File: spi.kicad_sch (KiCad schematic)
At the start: 3 parts, among them J3 Micro_SD_Card

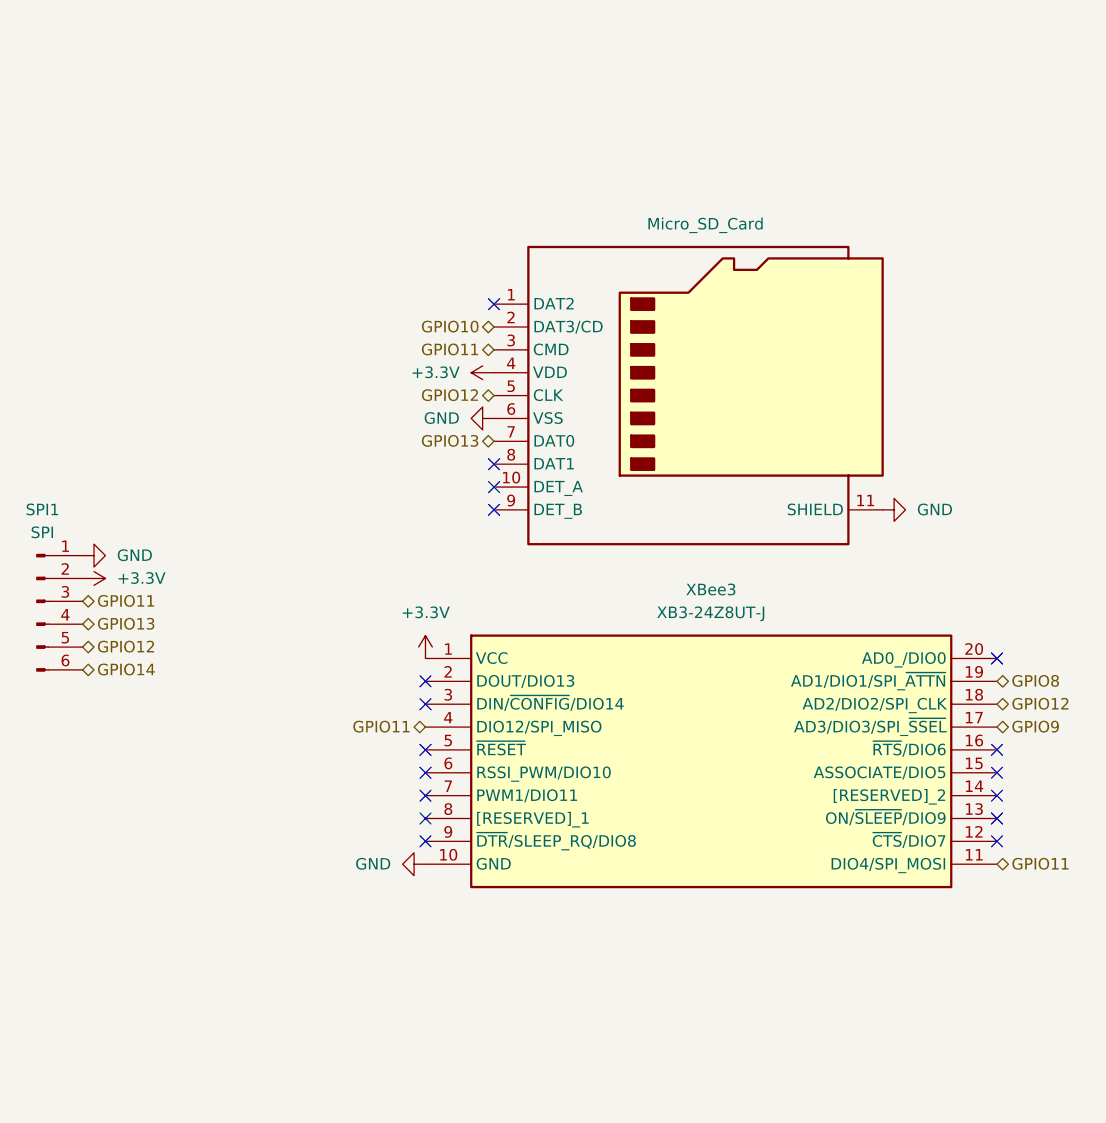
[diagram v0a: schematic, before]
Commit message: Remapped GPIOs for clean routing
This updates the GPIO table so that the traces and vias are far cleaner. Slight repositioning of some pins to account for that. Rebuilt all gerbers and necessary stuff.
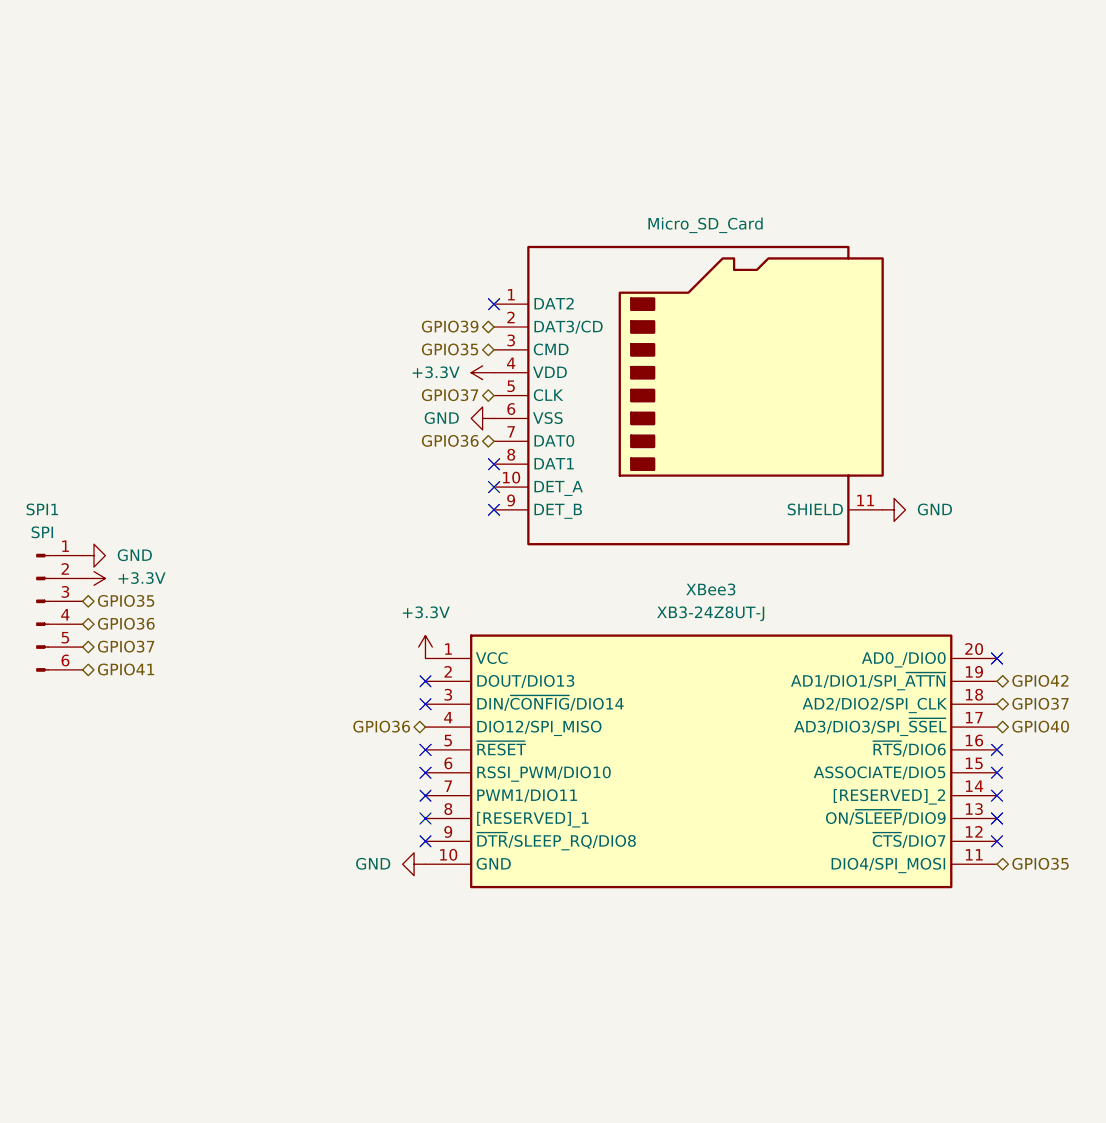
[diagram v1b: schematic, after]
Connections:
- net GPIO10 renamed GPIO39
- net GPIO11 renamed GPIO35
- net GPIO35: no longer XBee3.4 (DIO12/SPI_MISO)
- net GPIO12 renamed GPIO37
- net GPIO13 renamed GPIO36
- net GPIO36: now also XBee3.4 (DIO12/SPI_MISO)
- net GPIO14 renamed GPIO41
- net GPIO8 renamed GPIO42
- net GPIO9 renamed GPIO40
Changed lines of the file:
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@@
 		(at 110.49 100.33)
 	)
-	(hierarchical_label "GPIO11"
+	(hierarchical_label "GPIO35"
 		(shape bidirectional)
 		(at 118.11 63.5 180)
@@
 			(justify right)
 		)
-		(property "GPIO11" ""
+		(property "GPIO35" ""
 			(at 118.11 64.77 0)
 			(effects
@@
 		)
 	)
-	(hierarchical_label "GPIO14"
+	(hierarchical_label "GPIO41"
 		(shape bidirectional)
 		(at 72.39 99.06 0)
@@
 			(justify left)
 		)
-		(property "GPIO14" ""
+		(property "GPIO41" ""
 			(at 72.39 100.33 0)
 			(effects
@@
 		)
 	)
-	(hierarchical_label "GPIO11"
+	(hierarchical_label "GPIO35"
 		(shape bidirectional)
 		(at 72.39 91.44 0)
@@
 			(justify left)
 		)
-		(property "GPIO11" ""
+		(property "GPIO35" ""
 			(at 72.39 92.71 0)
 			(effects
@@
 		)
 	)
-	(hierarchical_label "GPIO11"
+	(hierarchical_label "GPIO40"
+		(shape bidirectional)
+		(at 173.99 105.41 0)
+		(fields_autoplaced yes)
+		(effects
+			(font
+				(size 1.27 1.27)
+			)
+			(justify left)
+		)
+		(property "GPIO40" ""
+			(at 173.99 106.68 0)
+			(effects
+				(font
+					(size 1.27 1.27)
+					(italic yes)
+				)
+				(justify left)
+			)
+		)
+	)
+	(hierarchical_label "GPIO36"
+		(shape bidirectional)
+		(at 110.49 105.41 180)
+		(fields_autoplaced yes)
+		(effects
+			(font
+				(size 1.27 1.27)
+			)
+			(justify right)
+		)
+		(property "GPIO36" ""
+			(at 110.49 106.68 0)
+			(effects
+				(font
+					(size 1.27 1.27)
+					(italic yes)
+				)
+				(justify right)
+			)
+		)
+	)
+	(hierarchical_label "GPIO35"
 		(shape bidirectional)
 		(at 173.99 120.65 0)
@@
 			(justify left)
 		)
-		(property "GPIO11" ""
+		(property "GPIO35" ""
 			(at 173.99 121.92 0)
 			(effects
@@
 		)
 	)
-	(hierarchical_label "GPIO9"
-		(shape bidirectional)
-		(at 173.99 105.41 0)
-		(fields_autoplaced yes)
-		(effects
-			(font
-				(size 1.27 1.27)
-			)
-			(justify left)
-		)
-		(property "GPIO9" ""
-			(at 173.99 106.68 0)
-			(effects
-				(font
-					(size 1.27 1.27)
-					(italic yes)
-				)
-				(justify left)
-			)
-		)
-	)
-	(hierarchical_label "GPIO11"
-		(shape bidirectional)
-		(at 110.49 105.41 180)
-		(fields_autoplaced yes)
-		(effects
-			(font
-				(size 1.27 1.27)
-			)
-			(justify right)
-		)
-		(property "GPIO11" ""
-			(at 110.49 106.68 0)
-			(effects
-				(font
-					(size 1.27 1.27)
-					(italic yes)
-				)
-				(justify right)
-			)
-		)
-	)
-	(hierarchical_label "GPIO13"
+	(hierarchical_label "GPIO36"
 		(shape bidirectional)
 		(at 72.39 93.98 0)
@@
 			(justify left)
 		)
-		(property "GPIO13" ""
+		(property "GPIO36" ""
 			(at 72.39 95.25 0)
 			(effects
@@
 		)
 	)
-	(hierarchical_label "GPIO13"
+	(hierarchical_label "GPIO36"
 		(shape bidirectional)
 		(at 118.11 73.66 180)
@@
 			(justify right)
 		)
-		(property "GPIO13" ""
+		(property "GPIO36" ""
 			(at 118.11 74.93 0)
 			(effects
@@
 		)
 	)
-	(hierarchical_label "GPIO12"
+	(hierarchical_label "GPIO37"
 		(shape bidirectional)
 		(at 173.99 102.87 0)
@@
 			(justify left)
 		)
-		(property "GPIO12" ""
+		(property "GPIO37" ""
 			(at 173.99 104.14 0)
 			(effects
@@
 		)
 	)
-	(hierarchical_label "GPIO10"
+	(hierarchical_label "GPIO39"
 		(shape bidirectional)
 		(at 118.11 60.96 180)
@@
 			(justify right)
 		)
-		(property "GPIO10" ""
+		(property "GPIO39" ""
 			(at 118.11 62.23 0)
 			(effects
@@
 		)
 	)
-	(hierarchical_label "GPIO8"
+	(hierarchical_label "GPIO42"
 		(shape bidirectional)
 		(at 173.99 100.33 0)
@@
 			(justify left)
 		)
-		(property "GPIO8" ""
+		(property "GPIO42" ""
 			(at 173.99 101.6 0)
 			(effects
@@
 		)
 	)
-	(hierarchical_label "GPIO12"
+	(hierarchical_label "GPIO37"
 		(shape bidirectional)
 		(at 118.11 68.58 180)
@@
 			(justify right)
 		)
-		(property "GPIO12" ""
+		(property "GPIO37" ""
 			(at 118.11 69.85 0)
 			(effects
@@
 		)
 	)
-	(hierarchical_label "GPIO12"
+	(hierarchical_label "GPIO37"
 		(shape bidirectional)
 		(at 72.39 96.52 0)
@@
 			(justify left)
 		)
-		(property "GPIO12" ""
+		(property "GPIO37" ""
 			(at 72.39 97.79 0)
 			(effects

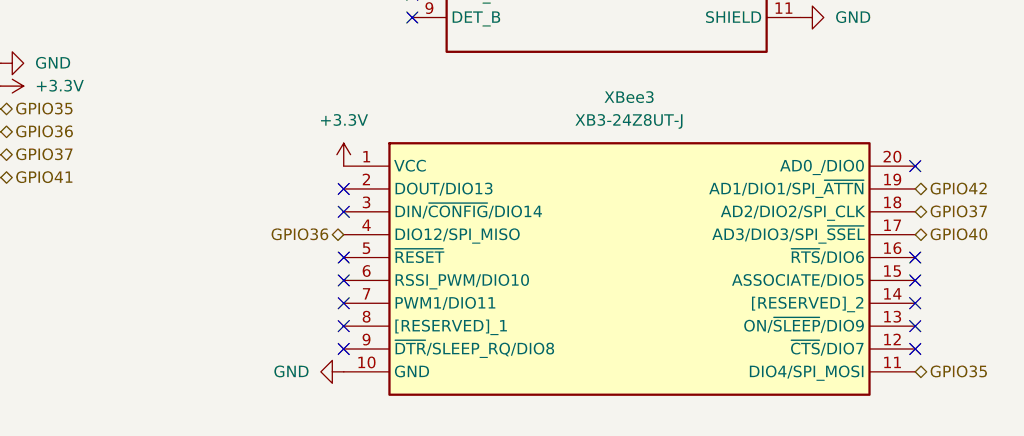
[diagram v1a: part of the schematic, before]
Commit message: final pass safety check
This verified that the XBee had all the pins wired up correctly with the proper resistor and cap connections. Glad I caught this before getting them fabbed.
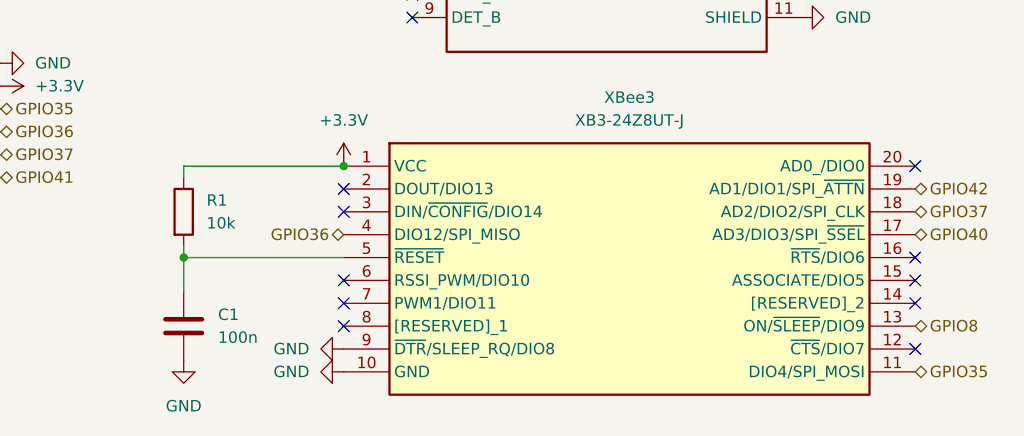
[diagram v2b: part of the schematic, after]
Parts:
- added C1: 100n, Capacitor_SMD:C_0603_1608Metric, symbol Device:C
- added R1: 10k, Resistor_SMD:R_0603_1608Metric, symbol Device:R
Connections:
- net +3.3V: now also R1.1
- net GND: now also XBee3.9 (~{DTR}/SLEEP_RQ/DIO8), C1.2
- net GPIO8: now reaches XBee3.13 (ON/~{SLEEP}/DIO9)
- net at XBee3.5 (~{RESET}): now also C1.1, R1.2
- no-connect marks 17 -> 14

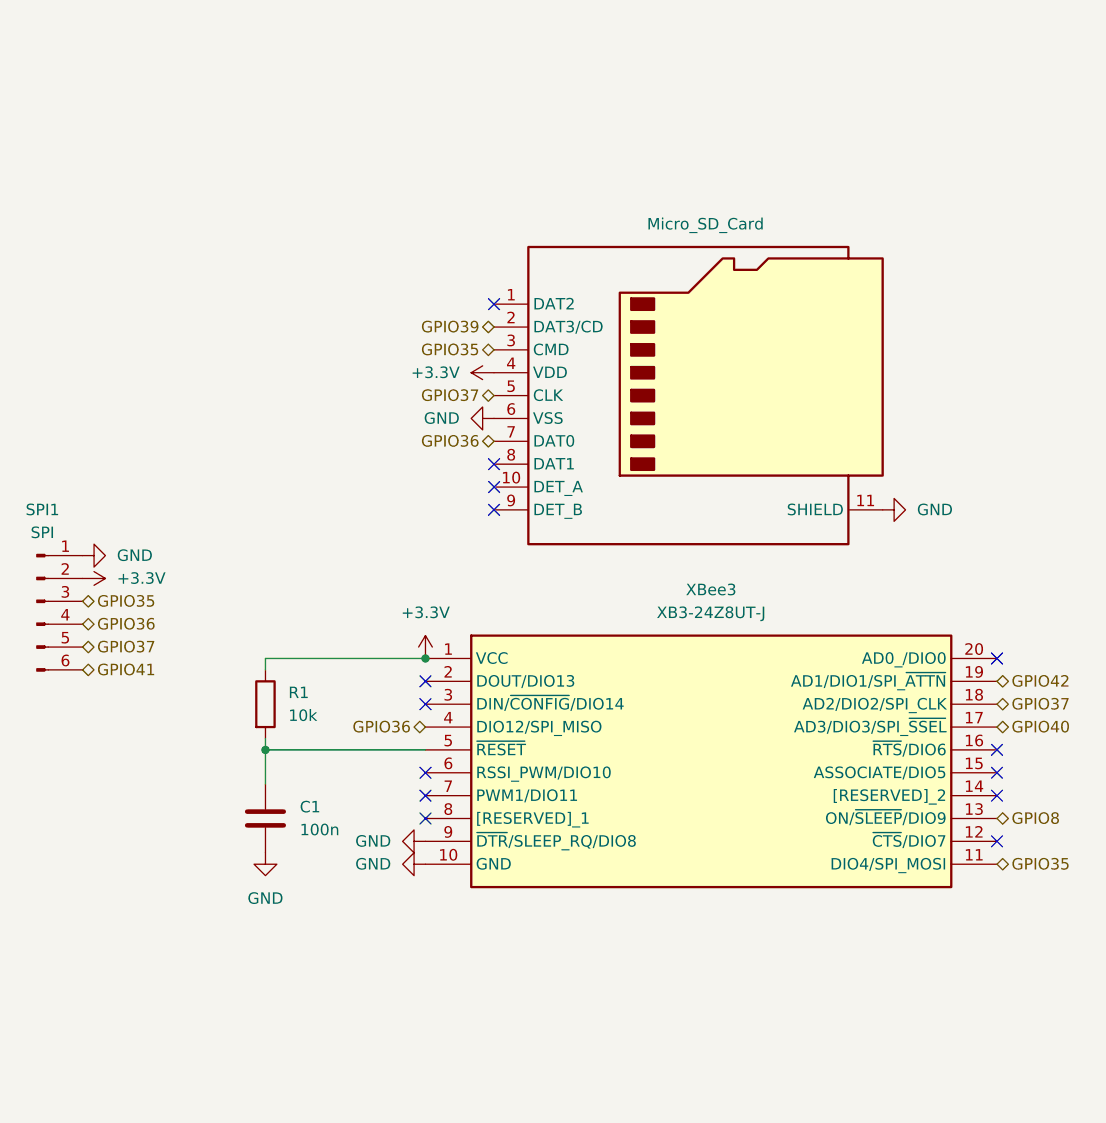
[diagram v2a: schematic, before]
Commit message: Updated to v1.1 to fix issues
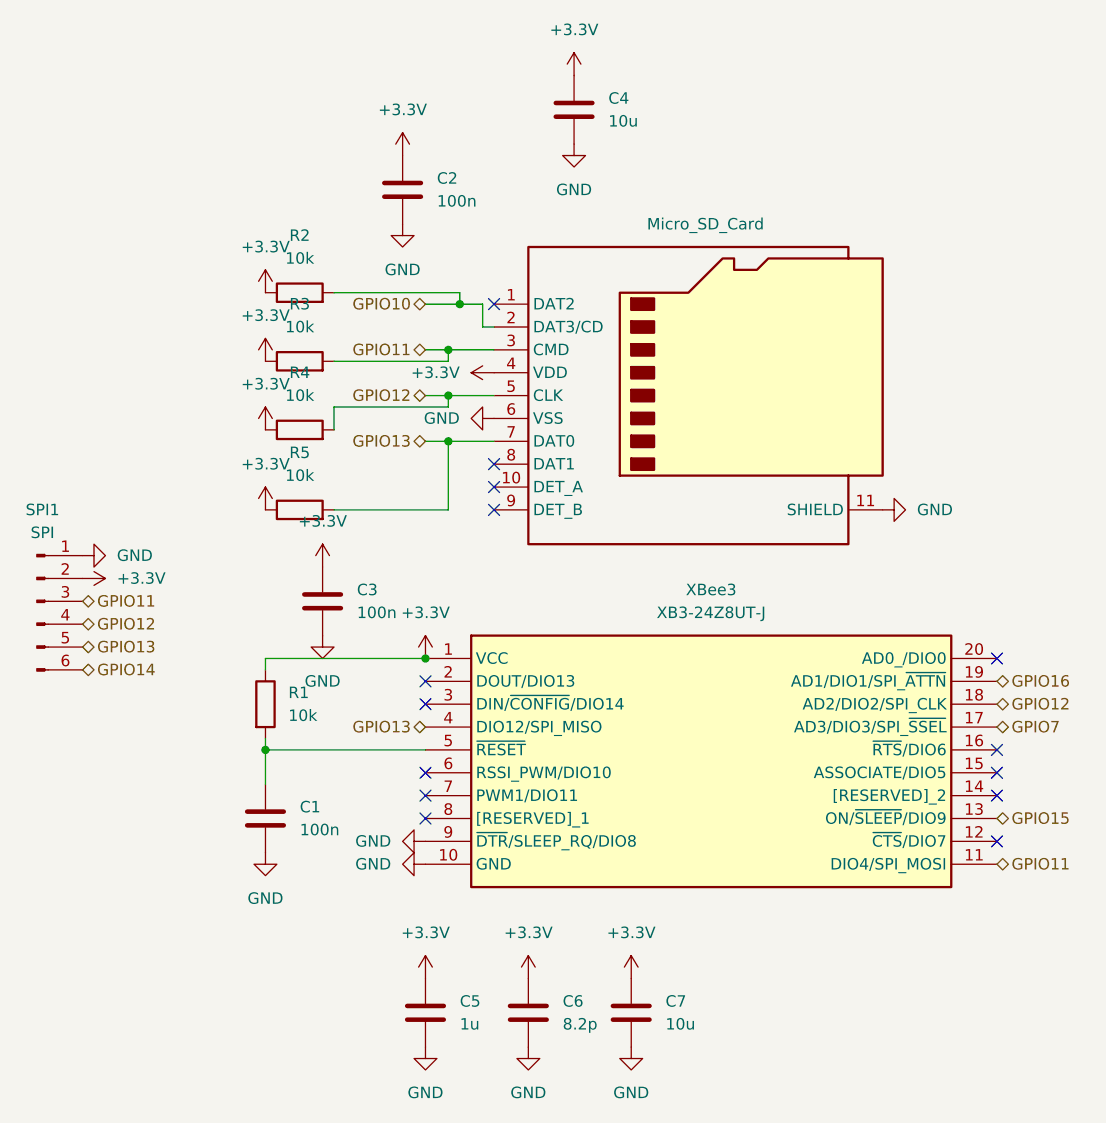
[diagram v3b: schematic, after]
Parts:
- added C2, C3: 100n, Capacitor_SMD:C_0603_1608Metric, symbol Device:C
- added C4, C7: 10u, Capacitor_SMD:C_0805_2012Metric, symbol Device:C
- added C5: 1u, Capacitor_SMD:C_0603_1608Metric, symbol Device:C
- added C6: 8.2p, Capacitor_SMD:C_0603_1608Metric, symbol Device:C
- added R2, R3, R4, R5: 10k, Resistor_SMD:R_0603_1608Metric, symbol Device:R
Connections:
- net +3.3V: now also C2.1, C3.1, C4.1, C5.1, C6.1, C7.1, R2.1, R3.1, R4.1, R5.1
- net GND: now also C2.2, C3.2, C4.2, C5.2, C6.2, C7.2
- net GPIO35 renamed GPIO11
- net GPIO11: now also R3.2
- net GPIO36 renamed GPIO13
- net GPIO13: now also SPI1.5 (Pin_5), R5.2; no longer SPI1.4 (Pin_4)
- net GPIO37 renamed GPIO12
- net GPIO12: now also SPI1.4 (Pin_4), R4.2; no longer SPI1.5 (Pin_5)
- net GPIO39 renamed GPIO10
- net GPIO10: now also R2.2
- net GPIO40 renamed GPIO7
- net GPIO41 renamed GPIO14
- net GPIO42 renamed GPIO16
- net GPIO8 renamed GPIO15

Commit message: Updated to v1.2 to address remaining issues
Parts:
- removed R4: 10k, Resistor_SMD:R_0603_1608Metric, symbol Device:R
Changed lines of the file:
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@@
 	)
 	(junction
-		(at 113.03 68.58)
-		(diameter 0)
-		(color 0 0 0 0)
-	)
-	(junction
 		(at 110.49 97.79)
 		(diameter 0)
@@
 	(wire
 		(pts
-			(xy 100.33 69.85) (xy 113.03 69.85)
-		)
-		(stroke
-			(width 0)
-			(type default)
-		)
-	)
-	(wire
-		(pts
 			(xy 113.03 81.28) (xy 113.03 73.66)
 		)
@@
 	(wire
 		(pts
-			(xy 100.33 72.39) (xy 100.33 69.85)
-		)
-		(stroke
-			(width 0)
-			(type default)
-		)
-	)
-	(wire
-		(pts
 			(xy 100.33 64.77) (xy 113.03 64.77)
 		)
@@
 	(wire
 		(pts
-			(xy 113.03 68.58) (xy 118.11 68.58)
+			(xy 110.49 68.58) (xy 118.11 68.58)
 		)
 		(stroke
@@
 	(wire
 		(pts
-			(xy 110.49 68.58) (xy 113.03 68.58)
-		)
-		(stroke
-			(width 0)
-			(type default)
-		)
-	)
-	(wire
-		(pts
-			(xy 113.03 68.58) (xy 113.03 69.85)
-		)
-		(stroke
-			(width 0)
-			(type default)
-		)
-	)
-	(wire
-		(pts
 			(xy 116.84 60.96) (xy 118.11 60.96)
 		)
@@
 	)
 	(symbol
-		(lib_id "Device:R")
-		(at 96.52 72.39 90)
-		(unit 1)
-		(exclude_from_sim no)
-		(in_bom yes)
-		(on_board yes)
-		(dnp no)
-		(fields_autoplaced yes)
-		(property "Reference" "R4"
-			(at 96.52 66.04 90)
-			(effects
-				(font
-					(size 1.27 1.27)
-				)
-			)
-		)
-		(property "Value" "10k"
-			(at 96.52 68.58 90)
-			(effects
-				(font
-					(size 1.27 1.27)
-				)
-			)
-		)
-		(property "Footprint" "Resistor_SMD:R_0603_1608Metric"
-			(at 96.52 74.168 90)
-			(effects
-				(font
-					(size 1.27 1.27)
-				)
-				(hide yes)
-			)
-		)
-		(property "Datasheet" "~"
-			(at 96.52 72.39 0)
-			(effects
-				(font
-					(size 1.27 1.27)
-				)
-				(hide yes)
-			)
-		)
-		(property "Description" "Resistor"
-			(at 96.52 72.39 0)
-			(effects
-				(font
-					(size 1.27 1.27)
-				)
-				(hide yes)
-			)
-		)
-		(pin "1"
-		)
-		(pin "2"
-		)
-		(instances
-			(project "AmidalaShield"
-				(path "/6d8d0000-f03d-4277-95db-0f566c3960c4/badd9ffd-b17a-400a-923e-2e73780848ba"
-					(reference "R4")
-					(unit 1)
-				)
-			)
-		)
-	)
-	(symbol
 		(lib_id "power:+3.3V")
 		(at 121.92 133.35 0)
@@
 					(unit 1)
 				)
-			)
-		)
-	)
-	(symbol
-		(lib_id "power:+3.3V")
-		(at 92.71 72.39 0)
-		(unit 1)
-		(exclude_from_sim no)
-		(in_bom yes)
-		(on_board yes)
-		(dnp no)
-		(fields_autoplaced yes)
-		(property "Reference" "#PWR023"
-			(at 92.71 76.2 0)
-			(effects
-				(font
-					(size 1.27 1.27)
-				)
-				(hide yes)
-			)
-		)
-		(property "Value" "+3.3V"
-			(at 92.71 67.31 0)
-			(effects
-				(font
-					(size 1.27 1.27)
-				)
-			)
-		)
-		(property "Footprint" ""
-			(at 92.71 72.39 0)
-			(effects
-				(font
-					(size 1.27 1.27)
-				)
-				(hide yes)
-			)
-		)
-		(property "Datasheet" ""
-			(at 92.71 72.39 0)
-			(effects
-				(font
-					(size 1.27 1.27)
-				)
-				(hide yes)
-			)
-		)
-		(property "Description" "Power symbol creates a global label with name \"+3.3V\""
-			(at 92.71 72.39 0)
-			(effects
-				(font
-					(size 1.27 1.27)
-				)
-				(hide yes)
-			)
-		)
-		(pin "1"
-		)
-		(instances
-			(project "AmidalaShield"
-				(path "/6d8d0000-f03d-4277-95db-0f566c3960c4/badd9ffd-b17a-400a-923e-2e73780848ba"
-					(reference "#PWR023")
-					(unit 1)
-				)
